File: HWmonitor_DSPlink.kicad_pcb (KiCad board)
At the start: 2 copper layers, 0 parts

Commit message: all footprints assigned
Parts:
- added C1: 100nF/50V, Capacitor_SMD:C_0603_1608Metric, F.Cu at (210.0, 103.5)
- added C10: 100nF/50V, Capacitor_SMD:C_0603_1608Metric, F.Cu at (223.8, 86.9)
- added C11: 100nF/50V, Capacitor_SMD:C_0603_1608Metric, F.Cu at (239.9, 89.8)
- added C12: 100nF/50V, Capacitor_SMD:C_0603_1608Metric, F.Cu at (206.0, 103.0)
- added C13: 100nF/50V, Capacitor_SMD:C_0603_1608Metric, F.Cu at (226.8, 97.0)
- added C14: 100nF/50V, Capacitor_SMD:C_0603_1608Metric, F.Cu at (226.8, 104.5)
- added C15: 10uF/16V, Capacitor_SMD:C_0805_2012Metric, F.Cu at (211.0, 95.8)
- added C16: 10uF/16V, Capacitor_SMD:C_0805_2012Metric, F.Cu at (206.6, 100.3)
- added C17: 10uF/16V, Capacitor_SMD:C_0805_2012Metric, F.Cu at (223.1, 84.2)
- added C18: 10uF/16V, Capacitor_SMD:C_0805_2012Metric, F.Cu at (206.6, 97.3)
- added C19: 100nF/50V, Capacitor_SMD:C_0603_1608Metric, F.Cu at (239.9, 92.3)
- added C2: 10uF/16V, Capacitor_SMD:C_0603_1608Metric, F.Cu at (223.8, 89.4)
- added C20: 100nF/50V, Capacitor_SMD:C_0603_1608Metric, F.Cu at (235.6, 95.3)
- added C21: 100nF/50V, Capacitor_SMD:C_0603_1608Metric, F.Cu at (230.8, 100.3)
- added C22: 100nF/50V, Capacitor_SMD:C_0603_1608Metric, F.Cu at (210.8, 101.0)
- added C23: 100nF/50V, Capacitor_SMD:C_0603_1608Metric, F.Cu at (235.3, 82.7)
- added C24: 68pF/50V, Capacitor_SMD:C_0603_1608Metric, F.Cu at (227.8, 89.0)
- added C25: 68pF/50V, Capacitor_SMD:C_0603_1608Metric, F.Cu at (236.4, 79.8)
- added C26: 68pF/50V, Capacitor_SMD:C_0603_1608Metric, F.Cu at (218.8, 98.2)
- added C27: 68pF/50V, Capacitor_SMD:C_0603_1608Metric, F.Cu at (223.6, 91.9)
- added C28: 100nF/50V, Capacitor_SMD:C_0603_1608Metric, F.Cu at (214.8, 101.0)
- added C29: 100nF/50V, Capacitor_SMD:C_0603_1608Metric, F.Cu at (240.6, 74.8)
- added C3: NM, Capacitor_SMD:C_0603_1608Metric, F.Cu at (210.8, 98.5)
- added C30: 100nF/50V, Capacitor_SMD:C_0603_1608Metric, F.Cu at (236.6, 77.3)
- added C31: 100nF/50V, Capacitor_SMD:C_0603_1608Metric, F.Cu at (227.8, 86.5)
- added C32: 100nF/50V, Capacitor_SMD:C_0603_1608Metric, F.Cu at (231.8, 80.2)
- added C33: 100nF/50V, Capacitor_SMD:C_0603_1608Metric, F.Cu at (219.3, 95.7)
- added C34: 100nF/50V, Capacitor_SMD:C_0603_1608Metric, F.Cu at (231.3, 82.7)
- added C35: 100nF/50V, Capacitor_SMD:C_0603_1608Metric, F.Cu at (219.5, 93.2)
- added C4: NM, Capacitor_SMD:C_0603_1608Metric, F.Cu at (227.3, 84.0)
- added C5: 100nF/50V, Capacitor_SMD:C_0603_1608Metric, F.Cu at (215.2, 95.4)
- added C6: 100nF/50V, Capacitor_SMD:C_0603_1608Metric, F.Cu at (219.6, 90.7)
- added C7: NM, Capacitor_SMD:C_0603_1608Metric, F.Cu at (232.4, 77.7)
- added C8: NM, Capacitor_SMD:C_0603_1608Metric, F.Cu at (236.6, 74.8)
- added C9: 10uF/16V, Capacitor_SMD:C_0805_2012Metric, F.Cu at (211.0, 92.8)
- added D1: BAV99, Package_TO_SOT_SMD:SOT-23, F.Cu at (218.7, 84.2)
- added D10: LED, LED_THT:LED_D3.0mm_FlatTop, F.Cu at (157.0, 109.5)
- added D11: D_Schottky, Diode_SMD:D_SOD-323, F.Cu at (219.7, 88.0)
- added D12: D_Schottky, Diode_SMD:D_SOD-323, F.Cu at (232.5, 75.0)
- added D2: D_Schottky, Diode_SMD:D_SOD-323F, F.Cu at (227.6, 79.6)
- added D3: BAV99, Package_TO_SOT_SMD:SOT-23, F.Cu at (223.3, 80.4)
- added D4: D_Zener, Diode_SMD:D_SOD-323F, F.Cu at (215.4, 92.7)
- added D5: LED, LED_THT:LED_D3.0mm_FlatTop, F.Cu at (122.5, 112.5)
- added D6: BAV99, Package_TO_SOT_SMD:SOT-23, F.Cu at (206.6, 93.6)
- added D7: BAV99, Package_TO_SOT_SMD:SOT-23, F.Cu at (215.3, 89.0)
- added D8: BAV99, Package_TO_SOT_SMD:SOT-23, F.Cu at (228.1, 75.8)
- added D9: LED, LED_THT:LED_D3.0mm_FlatTop, F.Cu at (152.0, 109.5)
- added J1: USB_B_Mini, Connector_USB:USB_Mini-B_Lumberg_2486_01_Horizontal, F.Cu at (169.0, 111.0)
- added J2: Conn_02x04_Odd_Even, Connector_IDC:IDC-Header_2x04_P2.54mm_Vertical, F.Cu at (122.0, 88.0)
- added J3: Conn_Coaxial, #MyLibrary:Connector_131-3701-301, F.Cu at (169.5, 88.5)
- added J4: Conn_Coaxial, #MyLibrary:Connector_131-3701-301, F.Cu at (169.5, 79.5)
- added J5: Conn_Coaxial, #MyLibrary:Connector_131-3701-301, F.Cu at (169.5, 98.5)
- added J6: Conn_Coaxial, #MyLibrary:Connector_131-3701-301, F.Cu at (169.5, 69.5)
- added L1: 0603, Inductor_SMD:L_0603_1608Metric, F.Cu at (223.5, 94.4)
- added R1: 10R, Resistor_SMD:R_0603_1608Metric, F.Cu at (235.8, 87.8)
- added R10: 750R, Resistor_SMD:R_0603_1608Metric, F.Cu at (231.8, 87.8)
- added R11: 10R, Resistor_SMD:R_0603_1608Metric, F.Cu at (218.8, 100.7)
- added R12: 10R, Resistor_SMD:R_0603_1608Metric, F.Cu at (227.8, 91.5)
- added R13: 10R, Resistor_SMD:R_0603_1608Metric, F.Cu at (231.8, 85.2)
- added R14: 10R, Resistor_SMD:R_0603_1608Metric, F.Cu at (214.0, 103.5)
- added R15: 10k, Resistor_SMD:R_0603_1608Metric, F.Cu at (240.6, 77.3)
- added R16: 10k, Resistor_SMD:R_0603_1608Metric, F.Cu at (227.6, 94.0)
- added R17: 10k, Resistor_SMD:R_0603_1608Metric, F.Cu at (214.8, 98.5)
- added R18: 10k, Resistor_SMD:R_0603_1608Metric, F.Cu at (226.8, 102.0)
- added R19: 10k, Resistor_SMD:R_0603_1608Metric, F.Cu at (235.8, 92.8)
- added R2: 10R, Resistor_SMD:R_0603_1608Metric, F.Cu at (222.8, 100.7)
- added R20: 10k, Resistor_SMD:R_0603_1608Metric, F.Cu at (231.6, 95.3)
- added R21: 10k, Resistor_SMD:R_0603_1608Metric, F.Cu at (239.9, 87.3)
- added R22: 10k, Resistor_SMD:R_0603_1608Metric, F.Cu at (226.8, 99.5)
- added R23: 10R, Resistor_SMD:R_0603_1608Metric, F.Cu at (235.8, 90.3)
- added R24: 10R, Resistor_SMD:R_0603_1608Metric, F.Cu at (222.8, 103.2)
- added R25: 10R, Resistor_SMD:R_0603_1608Metric, F.Cu at (239.9, 84.8)
- added R26: 10R, Resistor_SMD:R_0603_1608Metric, F.Cu at (231.8, 92.8)
- added R3: 27R, Resistor_SMD:R_0603_1608Metric, F.Cu at (231.8, 90.3)
- added R4: 10R, Resistor_SMD:R_0603_1608Metric, F.Cu at (235.8, 85.2)
- added R5: 10R, Resistor_SMD:R_0603_1608Metric, F.Cu at (230.8, 97.8)
- added R6: 10R, Resistor_SMD:R_0603_1608Metric, F.Cu at (218.8, 103.2)
- added R7: 10R, Resistor_SMD:R_0603_1608Metric, F.Cu at (239.4, 82.3)
- added R8: 270R, Resistor_SMD:R_0603_1608Metric, F.Cu at (240.4, 79.8)
- added R9: 270R, Resistor_SMD:R_0603_1608Metric, F.Cu at (222.8, 98.2)
- added T1: 760390014, #MyLibrary:Wuerth_760390014, F.Cu at (145.0, 101.5)
- added U1: FT232RL, Package_SO:SSOP-28_5.3x10.2mm_P0.65mm, F.Cu at (158.5, 117.0)
- added U10: OPA197xDBV, Package_TO_SOT_SMD:SOT-23-5, F.Cu at (223.5, 75.8)
- added U11: OPA197xDBV, Package_TO_SOT_SMD:SOT-23-5, F.Cu at (202.0, 97.2)
- added U2: ISO7830DWW, #MyLibrary:SOIC-16DWW, F.Cu at (135.5, 67.0)
- added U3: ISO7821DWW, #MyLibrary:SOIC-16DWW, F.Cu at (135.5, 116.5)
- added U4: SN6501, Package_TO_SOT_SMD:SOT-23-5, F.Cu at (210.7, 89.0)
- added U5: TL431DBZ, Package_TO_SOT_SMD:SOT-23, F.Cu at (201.8, 101.8)
- added U6: AD5324ARMZ, Package_SO:MSOP-10_3x3mm_P0.5mm, F.Cu at (148.5, 69.5)
- added U7: TLV70450DBVT, Package_TO_SOT_SMD:SOT-23-5, F.Cu at (144.0, 78.0)
- added U8: OPA197xDBV, Package_TO_SOT_SMD:SOT-23-5, F.Cu at (193.0, 74.1)
- added U9: OPA197xDBV, Package_TO_SOT_SMD:SOT-23-5, F.Cu at (192.0, 83.0)

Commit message: initial placement
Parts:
- removed J3, J4, J5, J6: Conn_Coaxial, #MyLibrary:Connector_131-3701-301
- added H1: MountingHole, MountingHole:MountingHole_3.2mm_M3, F.Cu at (170.4, 62.8)
- added H2: MountingHole, MountingHole:MountingHole_3.2mm_M3, F.Cu at (170.4, 120.8)
- added H3: MountingHole, MountingHole:MountingHole_3.2mm_M3, F.Cu at (121.4, 62.8)
- added H4: MountingHole, MountingHole:MountingHole_3.2mm_M3, F.Cu at (121.4, 120.8)
- added X1: Conn_Coaxial, #MyLibrary:Connector_131-3701-301, F.Cu at (169.1, 98.4)
- added X2: Conn_Coaxial, #MyLibrary:Connector_131-3701-301, F.Cu at (169.1, 89.5)
- added X3: Conn_Coaxial, #MyLibrary:Connector_131-3701-301, F.Cu at (169.1, 80.2)
- added X4: Conn_Coaxial, #MyLibrary:Connector_131-3701-301, F.Cu at (169.1, 70.3)
- moved C8 117.9 mm to (127.5, 119.6), turned to 90 degrees
- moved R7 115.6 mm to (125.5, 102.1)
- moved R1 114.3 mm to (121.8, 80.0), turned to 270 degrees
- moved R3 112.2 mm to (120.1, 80.0), turned to 90 degrees
- moved R5 108.7 mm to (123.6, 80.0), turned to 90 degrees
- moved R4 107.0 mm to (129.0, 79.3), turned to 180 degrees
- moved C7 106.0 mm to (126.6, 70.2)
- moved D3 105.6 mm to (121.5, 108.5), turned to 270 degrees
- moved D8 103.0 mm to (125.1, 74.4), turned to 90 degrees
- moved C4 102.0 mm to (126.6, 68.2)
- moved R2 101.4 mm to (121.4, 102.1), turned to 180 degrees
- moved D1 99.3 mm to (121.5, 104.6), turned to 270 degrees
- moved D2 98.7 mm to (128.9, 81.2), turned to 180 degrees
- moved R6 96.2 mm to (125.4, 80.0), turned to 90 degrees
- moved C2 95.5 mm to (129.0, 77.6)
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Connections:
- R12 pad 2: /VOUTA -> /VOUTB
- R13 pad 2: /VOUTA -> /VOUTC
- R14 pad 2: /VOUTA -> /VOUTD
- U2 pad 5: GND -> /SYNC_DSP
- U2 pad 9: (no net) -> GND
- U3 pad 5: GNDA -> /RXD_DSP
- U3 pad 9: (no net) -> GNDA
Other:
- board outline added: 55 x 64 mm

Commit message: placement, added USB input protection
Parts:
- added R27: 47R, Resistor_SMD:R_0603_1608Metric, F.Cu at (160.0, 112.6)
- added R28: 47R, Resistor_SMD:R_0603_1608Metric, F.Cu at (160.0, 115.7)
- added U12: USBLC6-2SC6, Package_TO_SOT_SMD:SOT-23-6, F.Cu at (162.8, 113.3)
- moved C10 10.4 mm to (163.3, 117.6), turned to 0 degrees
- moved C1 8.91 mm to (160.0, 119.8)
- moved R8 8.77 mm to (158.7, 109.4)
- moved L1 6.71 mm to (163.3, 116.0), turned to 180 degrees
- moved U1 5.30 mm to (154.0, 117.3)
- moved C9 4.73 mm to (146.7, 109.8)
- moved R9 4.66 mm to (152.6, 109.5), turned to 270 degrees
- moved C14 4.03 mm to (149.7, 81.5)
- moved U7 3.99 mm to (149.8, 78.7)
- moved C3 3.36 mm to (126.6, 62.8)
- moved C4 3.36 mm to (126.6, 64.8)
- moved D9 3.11 mm to (155.6, 109.8), turned to 90 degrees
- moved C24 3.10 mm to (155.9, 99.2)
- moved C32 3.10 mm to (158.6, 100.5)
- moved R19 3.10 mm to (161.3, 96.5)
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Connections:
- C1 pad 1: +5VA -> GNDA
- C1 pad 2: GNDA -> +5VA
- U1 pad 15: Net-(J1-Pad3) -> Net-(R27-Pad1)
- U1 pad 16: Net-(J1-Pad2) -> Net-(R28-Pad1)
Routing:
- added copper zone on B.Cu, net (none)
- added copper zone on B.Cu, net GND
- added copper zone on B.Cu, net GNDD
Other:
- board size 55 x 64 mm -> 55 x 66 mm

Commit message: some initial routing done
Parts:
- moved D1 5.20 mm to (121.6, 109.8), turned to 0 degrees
- moved D3 5.10 mm to (121.6, 113.6), turned to 0 degrees
- moved R7 4.55 mm to (121.4, 104.1), turned to 270 degrees
- moved R2 2.56 mm to (123.0, 104.1), turned to 90 degrees
- moved C7 1.22 mm to (126.8, 66.8), turned to 0 degrees
- moved C16 0.90 mm to (148.7, 93.6)
- moved C17 0.90 mm to (150.7, 93.6)
- moved D11 0.90 mm to (146.7, 93.6)
- moved D12 0.90 mm to (152.7, 93.6)
- moved C1 0.80 mm to (160.0, 119.0)
- moved C8 0.54 mm to (127.6, 120.1)
- moved C3 0.22 mm to (126.8, 62.7)
- moved C4 0.22 mm to (126.8, 64.7)
- moved C5 0.10 mm to (127.6, 60.3)
- turned R10 to 0 degrees
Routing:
- net GND: track 0.00 -> 39.5 mm, vias 0 -> 27
- net +5V: track 0.00 -> 30.2 mm, vias 0 -> 2
- net +5VA: track 0.00 -> 30.1 mm, vias 0 -> 1
- net GNDA: track 0.00 -> 28.5 mm, vias 0 -> 13
- net /VOUTA: track 0.00 -> 26.9 mm
- net GNDD: track 0.00 -> 18.2 mm, vias 0 -> 9
- net /VOUTB: track 0.00 -> 17.0 mm
- net /TXD_DSP: track 0.00 -> 15.0 mm
- net /REF2.5V: track 0.00 -> 14.5 mm
- net /TXD: track 0.00 -> 13.7 mm, vias 0 -> 2
- net Net-(R28-Pad1): track 0.00 -> 13.6 mm
- net /RXD_DSP: track 0.00 -> 13.4 mm
- net /RXD: track 0.00 -> 11.7 mm, vias 0 -> 2
- net +7.5V: track 0.00 -> 11.2 mm
- net -7.5V: track 0.00 -> 10.2 mm
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- added copper zone on B.Cu, net GNDA
- removed copper zone on B.Cu, net (none)

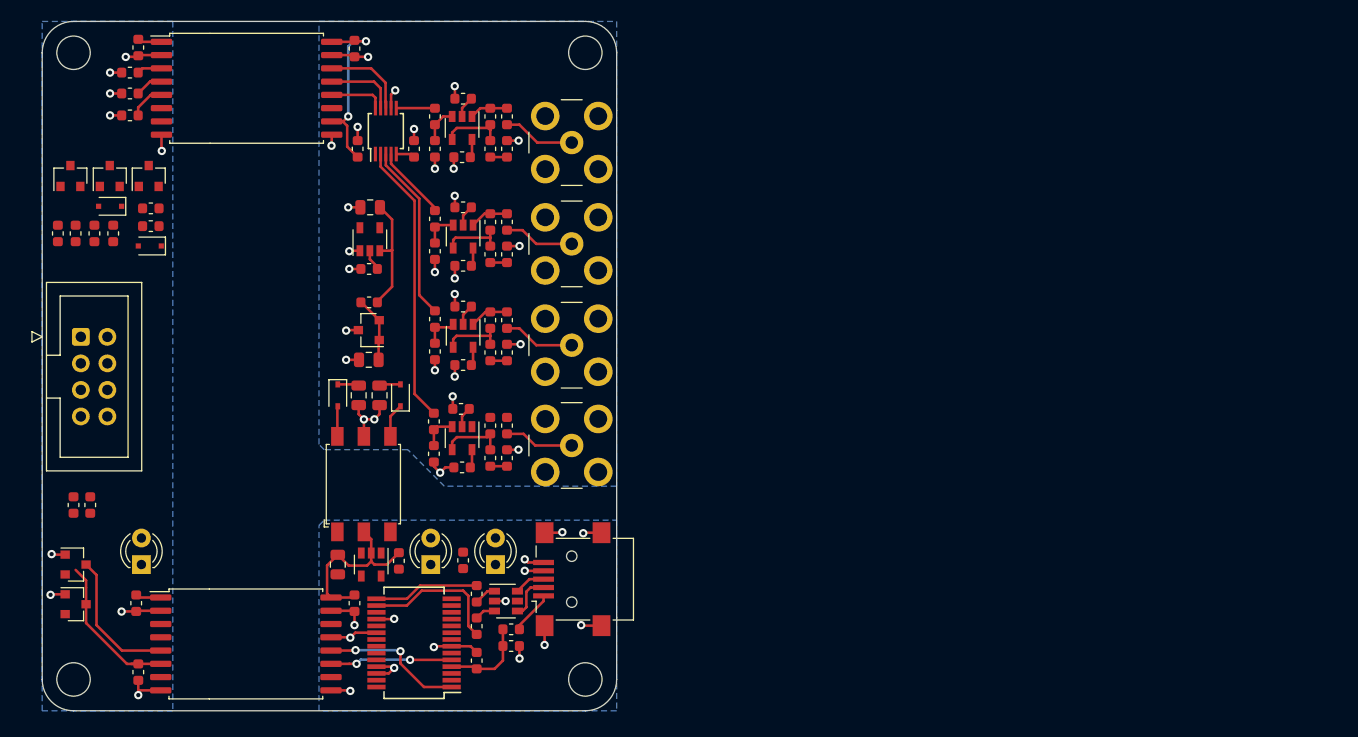
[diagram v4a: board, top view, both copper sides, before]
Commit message: two parts routed
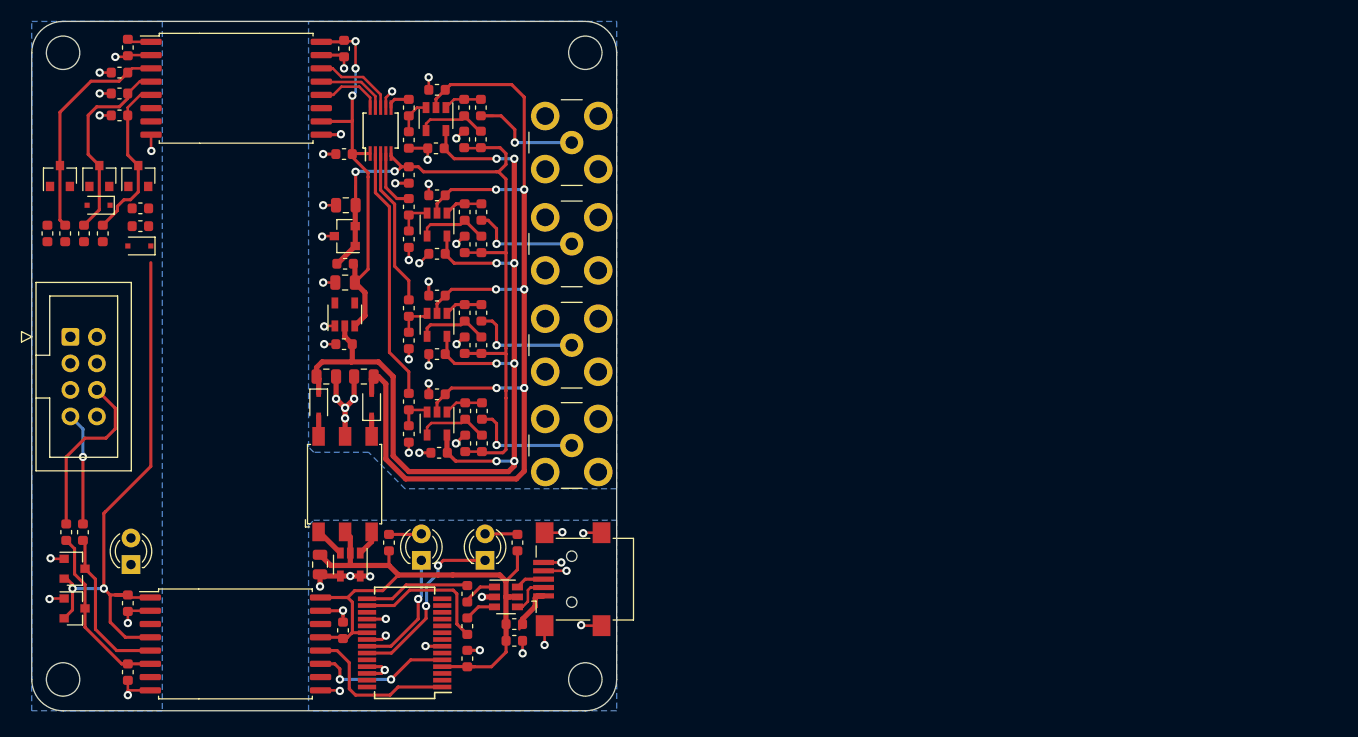
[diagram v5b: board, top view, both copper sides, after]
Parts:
- moved C15 15.0 mm to (147.5, 75.4)
- moved U5 9.29 mm to (147.4, 78.4)
- moved C18 7.59 mm to (147.4, 82.8)
- moved U7 7.59 mm to (147.4, 85.9)
- moved C14 7.59 mm to (147.3, 88.7)
- moved D10 7.11 mm to (154.7, 109.4)
- moved R8 5.47 mm to (163.9, 107.7)
- moved D9 5.22 mm to (160.8, 109.4)
- moved R10 4.36 mm to (147.4, 81.0)
- moved C20 4.24 mm to (158.9, 98.2)
- moved C23 4.20 mm to (158.8, 69.1)
- moved C22 4.16 mm to (158.9, 79.2)
- moved C21 4.11 mm to (158.9, 88.8)
- moved C16 3.58 mm to (145.6, 91.8), turned to 180 degrees
- moved C24 3.06 mm to (153.5, 97.3)
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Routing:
- net -7.5V: track 10.2 -> 100.7 mm, vias 0 -> 6
- net +7.5V: track 11.2 -> 100.5 mm, vias 0 -> 8
- net /REF2.5V: track 14.5 -> 72.6 mm, vias 0 -> 2
- net VD: track 4.73 -> 56.4 mm, vias 0 -> 2
- net +5VA: track 30.1 -> 69.9 mm, vias 1 -> 0
- net /DIN_DSP: track 2.40 -> 21.5 mm
- net /LED_TX: track 0.00 -> 17.5 mm, vias 0 -> 2
- net Net-(J2-Pad6): track 0.00 -> 16.7 mm
- net /SCLK_DSP: track 2.70 -> 19.2 mm
- net /SYNC_DSP: track 3.49 -> 16.2 mm
- net /LED_RX: track 0.00 -> 11.7 mm, vias 0 -> 1
- net Net-(J2-Pad7): track 0.00 -> 10.8 mm, vias 0 -> 1
- net +5V: track 30.2 -> 39.2 mm, vias 2 -> 3
- net GNDA: track 28.5 -> 35.5 mm, vias 13 -> 18
- net Net-(R26-Pad1): track 6.91 -> 11.7 mm, vias 0 -> 1
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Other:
- board size 55 x 66 mm -> 56 x 66 mm

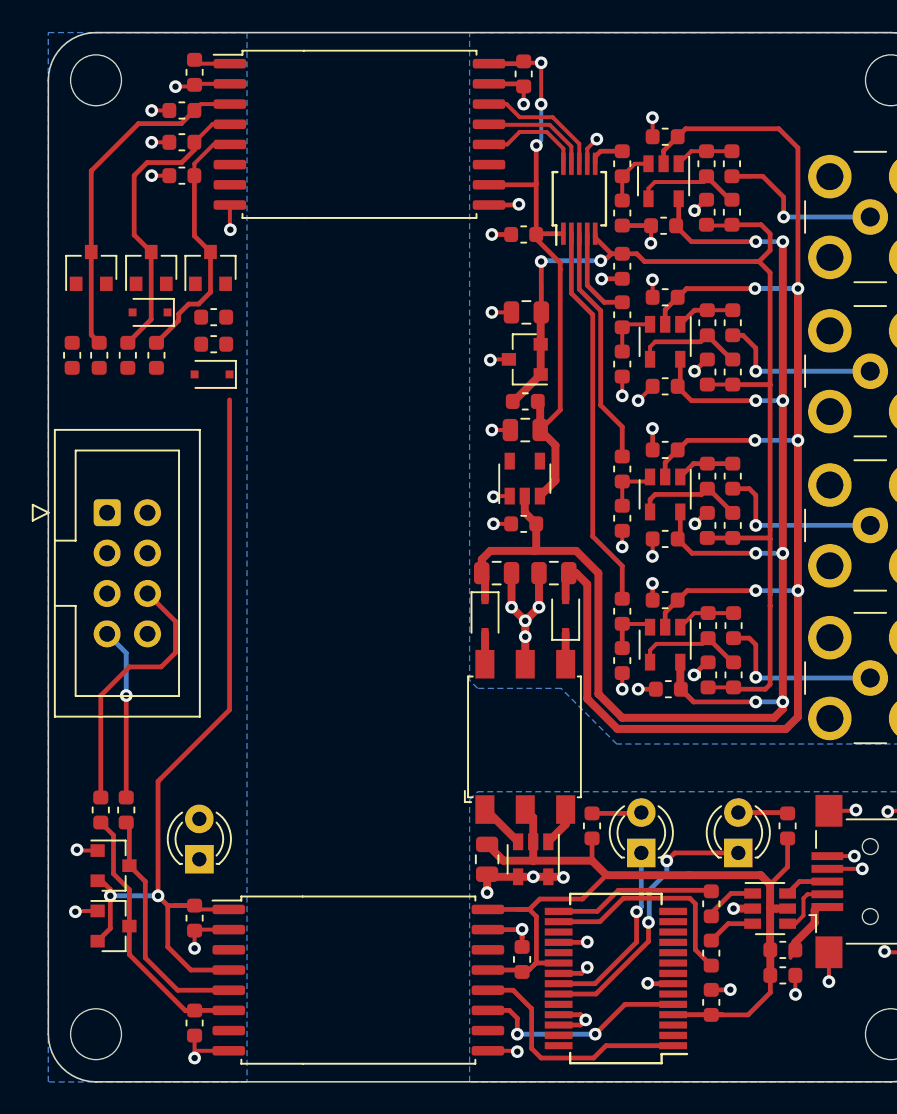
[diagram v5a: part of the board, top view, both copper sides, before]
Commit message: routing finished, added all MPNs
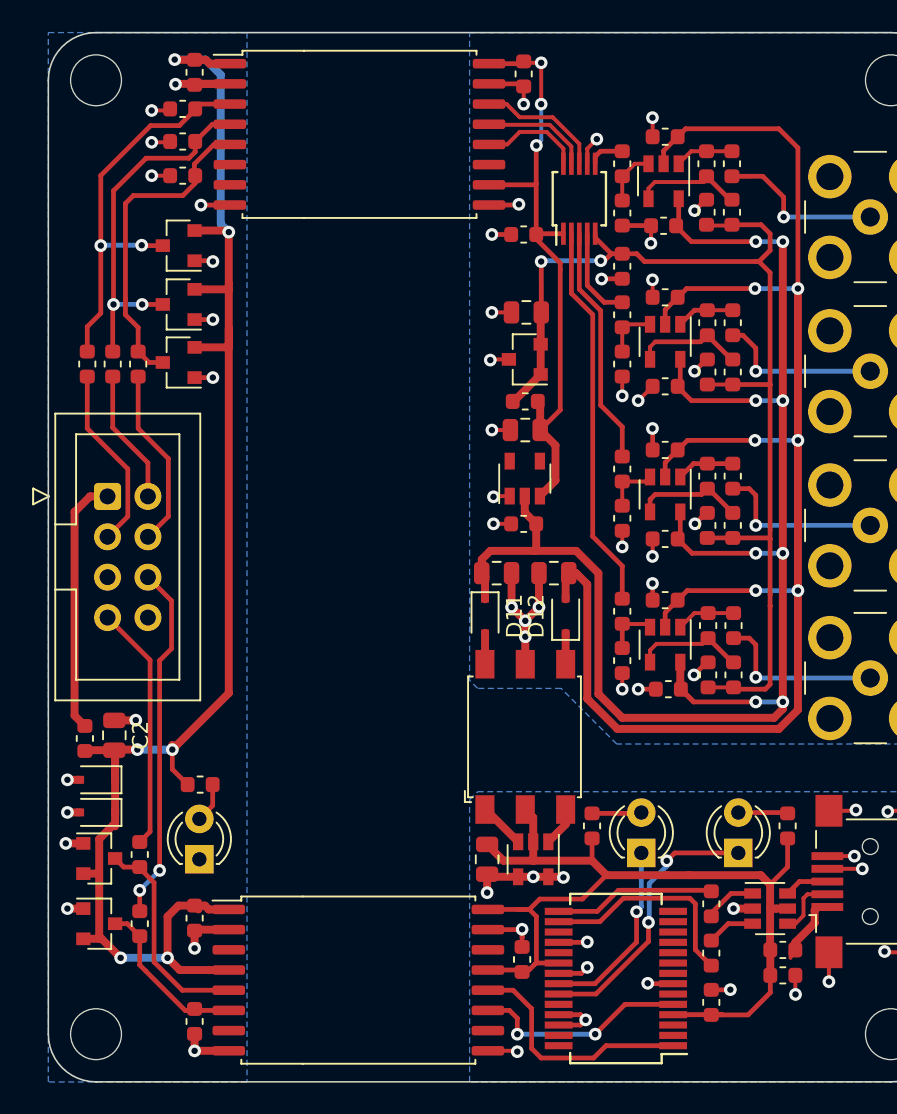
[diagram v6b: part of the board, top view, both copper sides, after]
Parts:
- C2: footprint Capacitor_SMD:C_0603_1608Metric -> Capacitor_SMD:C_0805_2012Metric
- D1, D3, D6, D7, D8: value BAV99 -> BAT54S
- D10, D5, D9: value LED -> RED
- D11, D12: value D_Schottky -> PMEG6010CEJ; footprint Diode_SMD:D_SOD-323 -> Diode_SMD:D_SOD-323F
- D2: value D_Schottky -> PMEG6010CEJ
- D4: value D_Zener -> 5.1V/200mW
- J1: value USB_B_Mini -> Mini USB - Type B
- J2: value Conn_02x04_Odd_Even -> IDC-Header 2x4
- L1: value 0603 -> 1k @100MHz
- U4: value SN6501 -> SN6501DBVR
- U5: value TL431DBZ -> TL431BCDBZ
- moved D4 31.6 mm to (120.5, 106.9)
- moved R4 27.7 mm to (127.0, 105.1), turned to 0 degrees
- moved C2 27.0 mm to (121.6, 102.0), turned to 270 degrees
- moved D2 26.5 mm to (120.5, 104.8)
- moved R3 24.1 mm to (119.7, 102.2), turned to 270 degrees
- moved R7 7.56 mm to (123.2, 113.9)
- moved D6 6.28 mm to (125.6, 78.6), turned to 180 degrees
- moved D7 5.68 mm to (125.6, 71.2), turned to 180 degrees
- moved R2 2.93 mm to (123.2, 109.5)
- moved D8 2.88 mm to (125.6, 74.9), turned to 180 degrees
- moved R6 1.27 mm to (123.1, 78.7)
- moved R5 1.10 mm to (121.5, 78.7)
- moved J2 1.03 mm to (121.2, 87.0)
- moved D1 1.01 mm to (120.6, 109.8)
- moved R1 0.93 mm to (119.9, 78.7)
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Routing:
- net VD: track 56.4 -> 101.4 mm, vias 2 -> 6
- net Net-(J2-Pad1): track 0.00 -> 16.2 mm
- net Net-(J2-Pad3): track 0.00 -> 11.7 mm
- net GNDD: track 17.9 -> 29.4 mm, vias 9 -> 15
- net Net-(J2-Pad4): track 0.00 -> 11.4 mm
- net Net-(J2-Pad2): track 0.00 -> 8.45 mm
- net /TXD_DSP: track 16.8 -> 10.5 mm
- net Net-(J2-Pad6): track 16.7 -> 22.8 mm, vias 0 -> 2
- net Net-(J2-Pad7): track 10.8 -> 15.5 mm, vias 1 -> 0
- net /SYNC_DSP: track 16.2 -> 20.3 mm
- net /DIN_DSP: track 21.5 -> 25.2 mm, vias 0 -> 2
- net /SCLK_DSP: track 19.2 -> 22.7 mm, vias 0 -> 2
- net Net-(D5-Pad2): track 0.00 -> 2.51 mm
- net /RXD_DSP: track 15.1 -> 13.6 mm
